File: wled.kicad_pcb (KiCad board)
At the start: 2 copper layers, 86.5 x 74.6 mm, 25 parts, among them J1 Audio pwr Selector, J2 Barrel_Jack_Switch, J3 Esp826, K1 FINDER-36.11, Q1 2N3904, U1 ESP32-DEVKIT-V1, U2 TSOP333xx

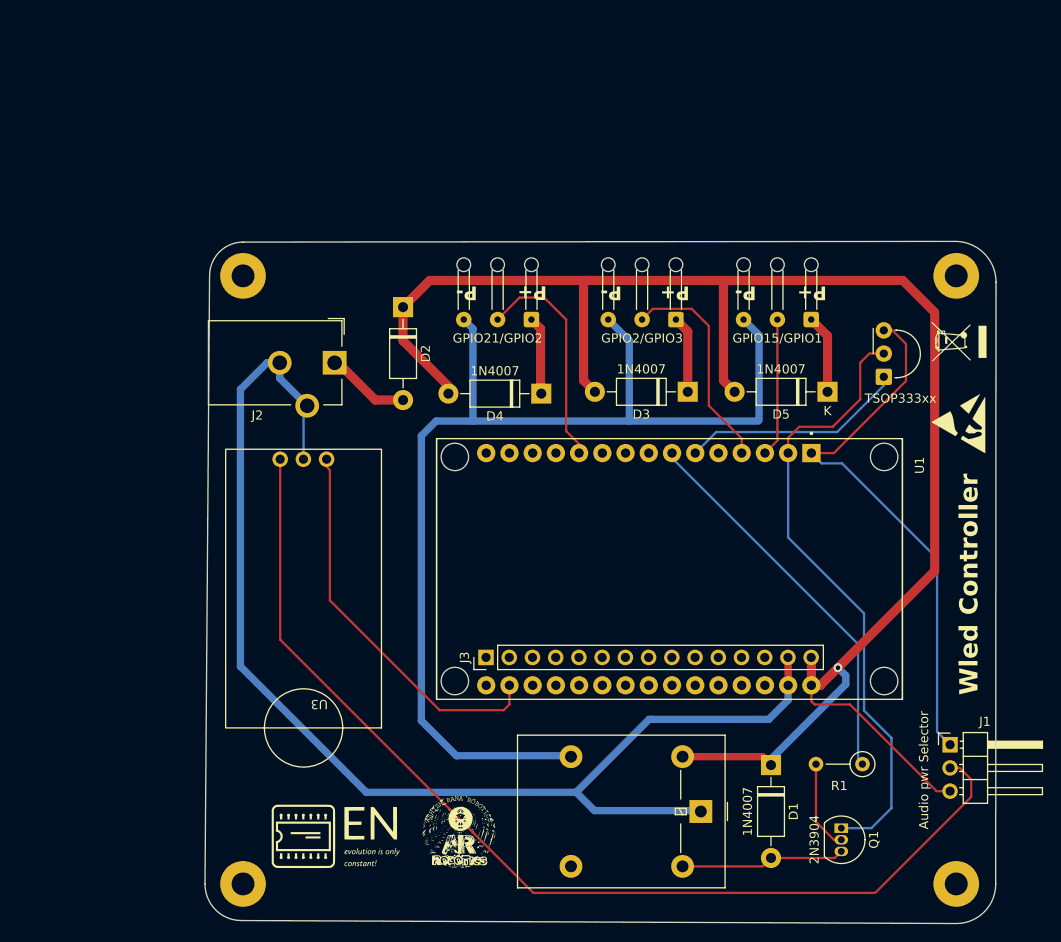
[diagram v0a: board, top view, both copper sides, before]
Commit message: New wled controller -smd with S3 Wroom-1 chip
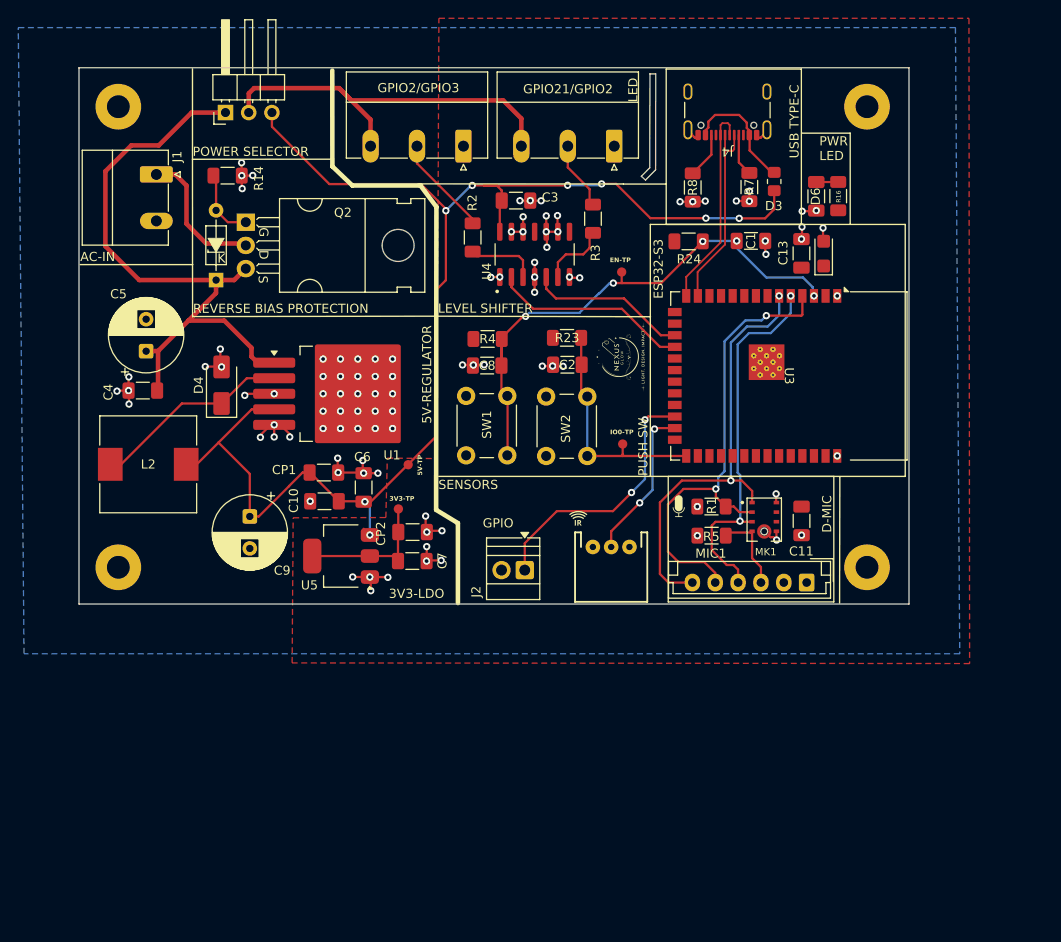
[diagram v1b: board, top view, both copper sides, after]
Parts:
- removed ? (x2): , LOGO
- removed D1, D2, D5: 1N4007, Diode_THT:D_DO-41_SOD81_P10.16mm_Horizontal
- removed GPIO15/GPIO1: L2, Connector_Wire:SolderWire-0.127sqmm_1x03_P3.7mm_D0.48mm_OD1mm_Relief
- removed K1: FINDER-36.11, Relay_THT:Relay_SPDT_Omron-G5LE-1
- removed Q1: 2N3904, Package_TO_SOT_THT:TO-92_Inline
- removed REF**: WEEE-Logo_4.2x6mm_SilkScreen, Symbol:WEEE-Logo_4.2x6mm_SilkScreen
- removed REF**: ESD-Logo_6.6x6mm_SilkScreen, Symbol:ESD-Logo_6.6x6mm_SilkScreen
- removed U2: TSOP333xx, OptoDevice:Vishay_MINIMOLD-3Pin
- added 100uf1: C_Tantalum, Capacitor_Tantalum_SMD:CP_EIA-3216-10_Kemet-I, F.Cu at (146.4, 58.0)
- added C1: 1uf, Capacitor_SMD:C_1206_3216Metric_Pad1.33x1.80mm_HandSolder, F.Cu at (138.4, 56.6)
- added C10: 100nF, Capacitor_SMD:C_1206_3216Metric_Pad1.33x1.80mm_HandSolder, F.Cu at (91.8, 85.1)
- added C11: 100nF, Capacitor_SMD:C_1206_3216Metric_Pad1.33x1.80mm_HandSolder, F.Cu at (143.9, 87.2)
- added C13: 0.1uF, Capacitor_SMD:C_1206_3216Metric_Pad1.33x1.80mm_HandSolder, F.Cu at (143.9, 58.0)
- added C2: 0u1f, Capacitor_SMD:C_1206_3216Metric_Pad1.33x1.80mm_HandSolder, F.Cu at (118.3, 70.1)
- added C3: C, Capacitor_SMD:C_1206_3216Metric_Pad1.33x1.80mm_HandSolder, F.Cu at (112.7, 52.2)
- added C4: 100nF, Capacitor_SMD:C_1206_3216Metric_Pad1.33x1.80mm_HandSolder, F.Cu at (71.9, 73.0)
- added C5: C_Polarized_Small, Capacitor_THT:CP_Radial_D8.0mm_P3.50mm, F.Cu at (72.3, 68.7)
- added C6: 100nF, Capacitor_SMD:C_1206_3216Metric_Pad1.33x1.80mm_HandSolder, F.Cu at (96.0, 83.6)
- added C7: 100nf, Capacitor_SMD:C_1206_3216Metric_Pad1.33x1.80mm_HandSolder, F.Cu at (101.4, 88.4)
- added C8: 0u1f, Capacitor_SMD:C_1206_3216Metric_Pad1.33x1.80mm_HandSolder, F.Cu at (109.6, 70.2)
- added C9: C_Polarized_Small, Capacitor_THT:CP_Radial_D8.0mm_P3.50mm, F.Cu at (83.6, 86.7)
- added CP1: 10uf, Capacitor_SMD:C_1206_3216Metric_Pad1.33x1.80mm_HandSolder, F.Cu at (91.7, 81.9)
- added CP2: 10uf, Capacitor_SMD:C_1206_3216Metric_Pad1.33x1.80mm_HandSolder, F.Cu at (101.4, 91.6)
- added D6: ESP-PWR, Capacitor_SMD:C_1206_3216Metric_Pad1.33x1.80mm_HandSolder, F.Cu at (145.6, 51.7)
- added DZ2: 1N5240B, PCM_Diode_THT_AKL:D_DO-35_SOD27_P7.62mm_Horizontal_Zener, F.Cu at (79.9, 60.9)
- added G***: LOGO, LOGO, F.Cu at (124.0, 69.3)
- added G***: LOGO, LOGO, F.Cu at (130.5, 85.6)
- added G***: LOGO, LOGO, F.Cu at (119.5, 86.9)
- added G***: LOGO, LOGO, B.Cu at (115.2, 60.7)
- added G***: LOGO, LOGO, B.Cu at (96.5, 87.0)
- added J4: USB_C_Receptacle_USB2.0_16P, Connector_USB:USB_C_Receptacle_GCT_USB4105-xx-A_16P_TopMnt_Horizontal, F.Cu at (135.8, 41.3)
- added L2: L, Inductor_SMD:L_10.4x10.4_H4.8, F.Cu at (72.5, 81.0)
- added MIC1: Conn_01x06_Pin, Connector_JST:JST_EH_B6B-EH-A_1x06_P2.50mm_Vertical, F.Cu at (144.5, 94.0)
- added MK1: INMP441ACEZ-R7, INMP441ACEZ-R7:MIC_INMP441ACEZ-R7, F.Cu at (139.9, 87.1)
- added PwrSelector1: Conn_01x03_Pin, Connector_PinHeader_2.54mm:PinHeader_1x03_P2.54mm_Horizontal, F.Cu at (80.9, 42.6)
- added Q2: AUIRF4905, PCM_Package_TO_SOT_THT_AKL:TO-220-3_Horizontal_TabDown_GDS, F.Cu at (83.2, 54.5)
- added R14: 100k, Resistor_SMD:R_1206_3216Metric_Pad1.30x1.75mm_HandSolder, F.Cu at (81.2, 49.5)
- added R16: 1k, Resistor_SMD:R_1206_3216Metric_Pad1.30x1.75mm_HandSolder, F.Cu at (147.9, 51.7)
- added R2: R, Resistor_SMD:R_1206_3216Metric_Pad1.30x1.75mm_HandSolder, F.Cu at (108.0, 56.2)
- added R23: 10k, Resistor_SMD:R_1206_3216Metric_Pad1.30x1.75mm_HandSolder, F.Cu at (118.3, 67.2)
- added R24: 10k, Resistor_SMD:R_1206_3216Metric_Pad1.30x1.75mm_HandSolder, F.Cu at (131.6, 56.6)
- added R3: R, Resistor_SMD:R_1206_3216Metric_Pad1.30x1.75mm_HandSolder, F.Cu at (121.1, 54.2)
- added R4: 10k, Resistor_SMD:R_1206_3216Metric_Pad1.30x1.75mm_HandSolder, F.Cu at (109.6, 67.3)
- added R5: 100k, Resistor_SMD:R_1206_3216Metric_Pad1.30x1.75mm_HandSolder, F.Cu at (134.1, 88.8)
- added R7: 5.1k, Resistor_SMD:R_1206_3216Metric_Pad1.30x1.75mm_HandSolder, F.Cu at (138.2, 50.7)
- added R8: 5.1k, Resistor_SMD:R_1206_3216Metric_Pad1.30x1.75mm_HandSolder, F.Cu at (132.0, 50.8)
- added SW1: SW_Push, Button_Switch_THT:SW_PUSH_6mm_H13mm, F.Cu at (107.3, 80.0)
- added SW2: SW_Push, Button_Switch_THT:SW_PUSH_6mm_H13mm, F.Cu at (116.0, 80.1)
- added TP1: TestPoint, PCM_SparkFun-Connector:TestPoint-1.0mm, F.Cu at (99.8, 85.9)
- added TP2: TestPoint, PCM_SparkFun-Connector:TestPoint-1.0mm, F.Cu at (100.9, 81.1)
- added TP3: TestPoint, PCM_SparkFun-Connector:TestPoint-1.0mm, F.Cu at (124.3, 60.0)
- added TP4: TestPoint, PCM_SparkFun-Connector:TestPoint-1.0mm, F.Cu at (124.4, 78.8)
- added U4: SN74HCT125DR, SN74HCT125DR:SOIC127P600X175-14N, F.Cu at (114.8, 58.1)
- added U5: AMS1117-3.3, Package_TO_SOT_SMD:SOT-223-3_TabPin2, F.Cu at (93.6, 91.1)
- D3: value 1N4007 -> D_Schottky; footprint Diode_THT:D_DO-41_SOD81_P10.16mm_Horizontal -> Resistor_SMD:R_0805_2012Metric_Pad1.20x1.40mm_HandSolder
- D4: value 1N4007 -> SS34; footprint Diode_THT:D_DO-41_SOD81_P10.16mm_Horizontal -> Diode_SMD:D_SMA
- GPIO2/GPIO3, GPIO21/GPIO2: footprint Connector_Wire:SolderWire-0.127sqmm_1x03_P3.7mm_D0.48mm_OD1mm_Relief -> Connector_Phoenix_MC_HighVoltage:PhoenixContact_MC_1,5_3-G-5.08_1x03_P5.08mm_Horizontal
- J1: value Audio pwr Selector -> Screw_Terminal_01x02; footprint Connector_PinHeader_2.54mm:PinHeader_1x03_P2.54mm_Horizontal -> Connector_Phoenix_MC_HighVoltage:PhoenixContact_MC_1,5_2-G-5.08_1x02_P5.08mm_Horizontal
- J2: value Barrel_Jack_Switch -> GPIO; footprint Connector_BarrelJack:BarrelJack_CUI_PJ-102AH_Horizontal -> TerminalBlock:TerminalBlock_Xinya_XY308-2.54-2P_1x02_P2.54mm_Horizontal
- J3: value Esp826 -> JST_2mm_3; footprint Connector_PinHeader_2.54mm:PinHeader_1x15_P2.54mm_Vertical -> PCM_SparkFun-Connector:JST_1x03_P2.0mm_Horizontal_PTH
- R1: value R -> 100k; footprint Resistor_THT:R_Axial_DIN0207_L6.3mm_D2.5mm_P5.08mm_Vertical -> Resistor_SMD:R_1206_3216Metric_Pad1.30x1.75mm_HandSolder
- U1: value ESP32-DEVKIT-V1 -> LM2596S-ADJ; footprint MODULE_ESP32_DEVKIT_V1:MODULE_ESP32_DEVKIT_V1 -> Package_TO_SOT_SMD:TO-263-5_TabPin3
- U3: value ~ -> ESP32-S3-WROOM-1; footprint sound sen:sound sens -> RF_Module:ESP32-S3-WROOM-1
- moved J1 106.9 mm to (73.4, 49.3), turned to -90 degrees
- moved H4 86.1 mm to (69.2, 41.9)
- moved U3 61.5 mm to (142.6, 71.4), turned to -90 degrees
- moved U1 40.4 mm to (93.9, 73.3), turned to 0 degrees
- moved H2 36.0 mm to (151.1, 92.3)
- moved D4 35.0 mm to (80.5, 72.4), turned to 90 degrees
- moved H3 34.7 mm to (69.2, 92.3)
- moved R1 32.7 mm to (134.1, 85.7), turned to 0 degrees
- moved J2 30.8 mm to (113.7, 92.6), turned to 180 degrees
- moved GPIO2/GPIO3 30.0 mm to (107.0, 46.2)
- moved D3 24.9 mm to (140.9, 50.1), turned to 90 degrees
- moved GPIO21/GPIO2 21.0 mm to (123.5, 46.2)
- moved H1 20.9 mm to (151.1, 41.9)
- moved J3 18.3 mm to (123.1, 90.1), turned to 180 degrees
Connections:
- net Net-(GPIO15/GPIO1-Pin_3) renamed /Vled
- D3 pad 1: Net-(D3-K) -> 5V
- D3 pad 2: Net-(D1-K) -> Net-(D3-A)
- D4 pad 2: Net-(D1-K) -> GND
- GPIO2/GPIO3 pad 1: Net-(D3-K) -> GND
- GPIO2/GPIO3 pad 2: Net-(GPIO2/GPIO3-Pin_2) -> /LED1
- GPIO21/GPIO2 pad 1: Net-(D4-K) -> GND
- GPIO21/GPIO2 pad 2: Net-(GPIO21/GPIO2-Pin_2) -> /LED2
- J1 pad 2: Net-(J1-Pin_2) -> GND
- J2 pad 1: Net-(D2-A) -> /GPIO
- J2 pad 2: Net-(J3-Pin_14) -> GND
- J3 pad 1: unconnected-(J3-Pin_1-Pad1) -> 3V3
- J3 pad 2: unconnected-(J3-Pin_2-Pad2) -> /ir
- J3 pad 3: unconnected-(J3-Pin_3-Pad3) -> GND
- R1 pad 1: Net-(U1-TX2) -> GND
- R1 pad 2: Net-(Q1-B) -> /SD
- U1 pad 1: Net-(J1-Pin_1) -> /12V
- U1 pad 2: Net-(Q1-E) -> Net-(D4-K)
- U1 pad 3: Net-(GPIO15/GPIO1-Pin_2) -> GND
- U1 pad 4: Net-(GPIO2/GPIO3-Pin_2) -> 5V
- U1 pad 5: unconnected-(U1-D4-Pad5) -> GND
- U3 pad 1: Net-(J1-Pin_2) -> GND
- U3 pad 2: Net-(J3-Pin_14) -> 3V3
- U3 pad 3: Net-(U1-VP) -> ESP32_EN
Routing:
- net Net-(D1-K): track 193.9 -> 0.00 mm, vias 1 -> 0
- net 5V: track 0.00 -> 150.9 mm, vias 0 -> 8
- net Net-(J3-Pin_14): track 137.5 -> 0.00 mm
- net Net-(J1-Pin_2): track 115.9 -> 0.00 mm
- net GND: track 0.00 -> 79.8 mm, vias 0 -> 102
- net /Vled: track 121.9 -> 44.3 mm
- net /12V: track 0.00 -> 69.3 mm
- net Net-(Q1-E): track 68.2 -> 0.00 mm
- net ESP32_EN: track 0.00 -> 59.5 mm, vias 0 -> 5
- net /SD: track 0.00 -> 52.3 mm, vias 0 -> 2
- net /SCK: track 0.00 -> 48.3 mm, vias 0 -> 2
- net Net-(J1-Pin_1): track 60.2 -> 16.1 mm
- net Net-(U1-TX2): track 43.2 -> 0.00 mm
- net Net-(U1-VP): track 42.5 -> 0.00 mm
- net /WS: track 0.00 -> 41.1 mm, vias 0 -> 2
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- added copper zone on F.Cu, net 3V3
- added copper zone on B.Cu, net GND
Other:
- board size 86.5 x 74.6 mm -> 90.8 x 58.7 mm
- board text added: "3V3-LDO"
- board text added: "3V3-TP"
- board text added: "5V-REGULATOR"
- board text added: "5V-TP"
- board text added: "AC-IN"
- board text added: "D-MIC"
- board text added: "EN-TP"
- board text added: "ESP32-S3"
- board text added: "GPIO"
- board text added: "I2S-MIC Conf."
- board text added: "IO0-TP"
- board text added: "LED"
- board text added: "LEVEL SHIFTER"
- board text added: "POWER SELECTOR"
- board text added: "PUSH SW"
- board text added: "PWR LED"
- board text added: "REVERSE BIAS PROTECTION"
- board text added: "SENSORS"
- board text added: "USB TYPE-C"
- board text removed: "P+"
- board text removed: "P-"
- board text removed: "Wled Controller"
